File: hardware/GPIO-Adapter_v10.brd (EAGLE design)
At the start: 55 x 20 mm, 8 parts, among them J1 FPC40_PIN, X1 PASSER, X2 PASSER, X3 PASSER, X4 PASSER

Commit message: updated docu and schematics
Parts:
- renumbered J1 to J1-TOP

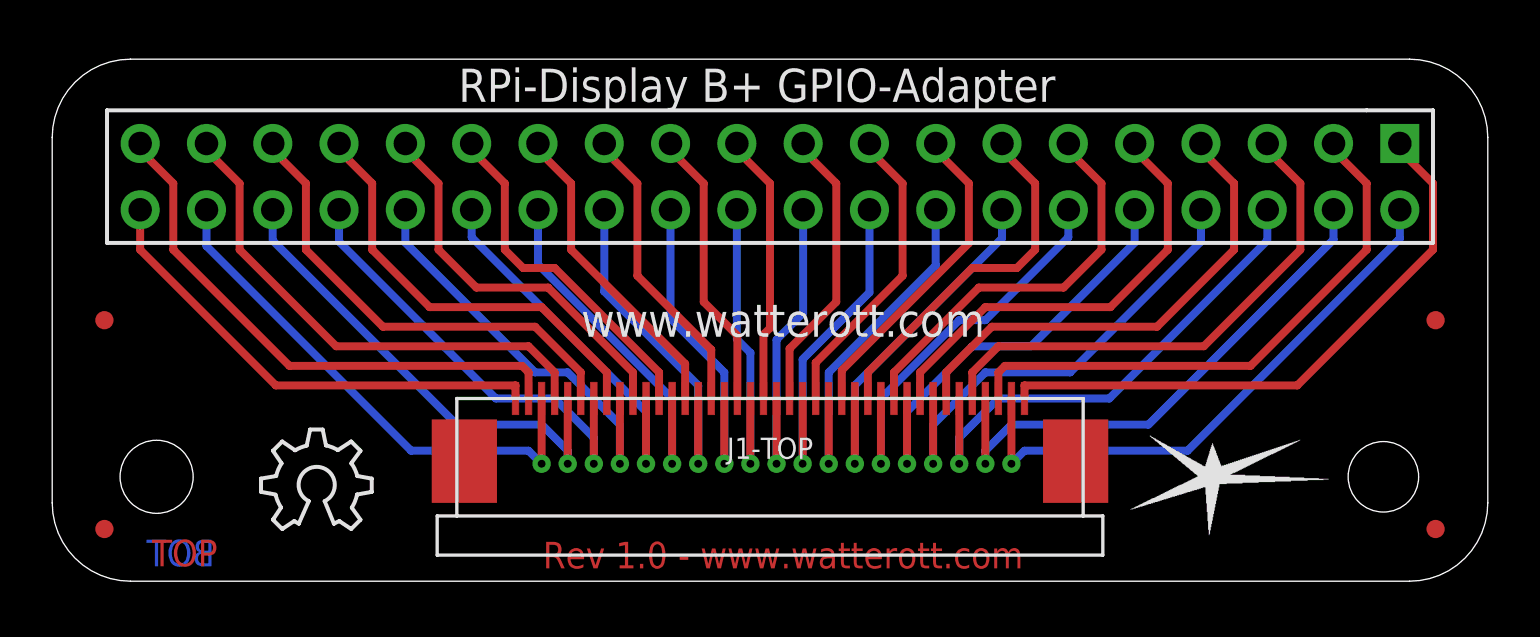
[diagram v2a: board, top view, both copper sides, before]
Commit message: updated schematics
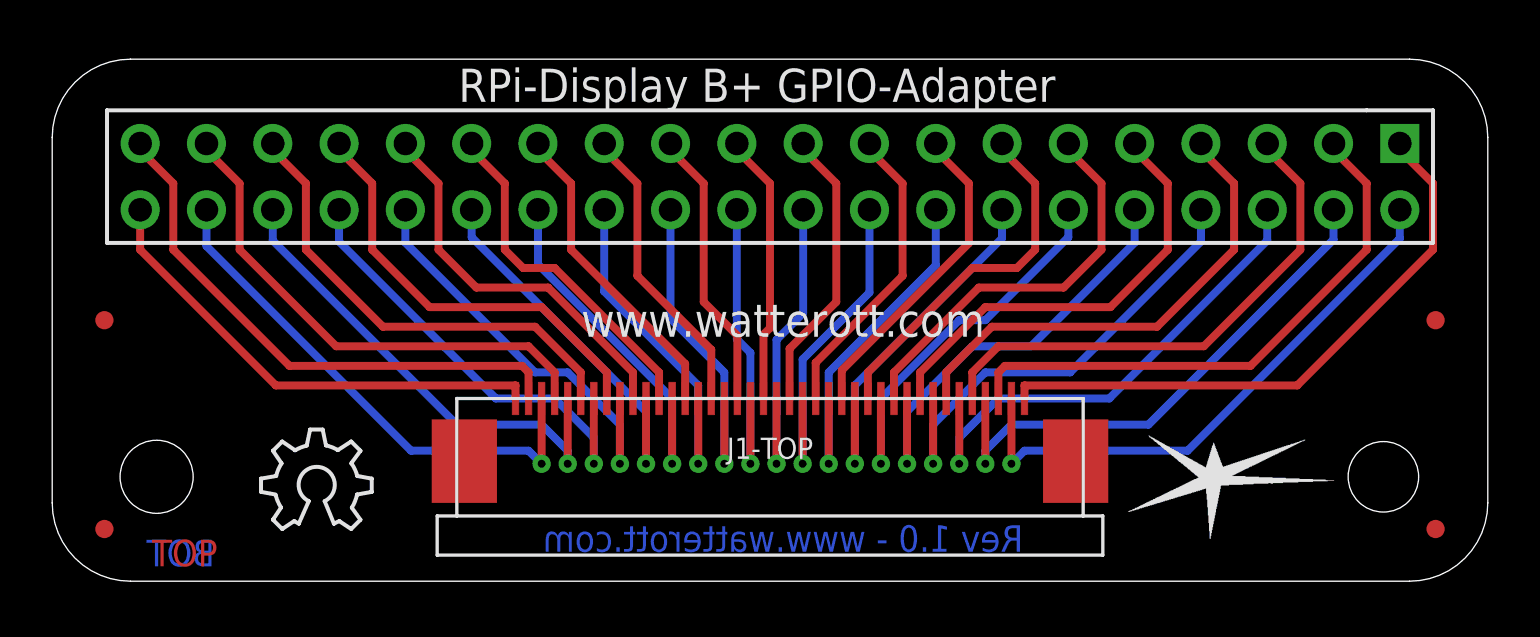
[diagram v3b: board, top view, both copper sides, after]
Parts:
- removed LOGO2: LOGO-S_PLACE_M, we-symbol:SPARK_TPLACE_M
- added LOGO3: LOGO_SPARK-4, we-symbol:SPARK_4MM
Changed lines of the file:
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@@
 <?xml version="1.0" encoding="utf-8"?>
 <!DOCTYPE eagle SYSTEM "eagle.dtd">
-<eagle version="7.5.0">
+<eagle version="7.7.0">
 <drawing>
 <settings>
@@
 <text x="-22.42" y="1.5875" size="1.016" layer="1" font="vector" ratio="20" rot="R180" align="bottom-center">TOP</text>
 <text x="-22.57875" y="1.5875" size="1.016" layer="16" font="vector" ratio="20" rot="MR0" align="top-center">BOT</text>
-<text x="0.5" y="1" size="1.016" layer="1" font="vector" ratio="20" align="center">Rev 1.0 - www.watterott.com</text>
+<text x="0.5" y="1.635" size="1.016" layer="16" font="vector" ratio="20" rot="MR0" align="center">Rev 1.0 - www.watterott.com</text>
 <text x="0.5" y="10" size="1.27" layer="21" font="vector" ratio="10" align="center">www.watterott.com</text>
 <wire x1="-24.5" y1="0" x2="24.5" y2="0" width="0" layer="20"/>
@@
 <attribute name="DIGIKEY_BOT" value="62684-401100AHLF-ND" x="0" y="7" size="1.778" layer="27" rot="R270" display="off"/>
 </element>
-<element name="LOGO2" library="we-symbol" package="SPARK_TPLACE_M" value="LOGO-S_PLACE_M" x="17" y="4"/>
+<element name="LOGO3" library="we-symbol" package="SPARK_4MM" value="LOGO_SPARK-4" x="17" y="4"/>
 </elements>
 <signals>
